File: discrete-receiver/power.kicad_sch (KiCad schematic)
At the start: 67 parts, among them J2 Optional 5V DC Jack, U11 Ag9905LP, U13 LM66100DCK, U14 LM66100DCK, U15 LM66100DCK

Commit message: Add components
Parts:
- removed R3: 49.9kΩ, PCM_JLCPCB:R_0402, symbol PCM_JLCPCB-Resistors:0402,49.9kΩ
- added C105: 100nF, PCM_JLCPCB:C_0402, symbol PCM_JLCPCB-Capacitors:0402,100nF
- added R3: 47kΩ, PCM_JLCPCB:R_0402, symbol PCM_JLCPCB-Resistors:0402,47kΩ
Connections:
- net at R10.1, U20.3 (FB): now also R3.2
- net at JP30.2 (B), R27.1, U20.1 (OUT)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: now also C105.2, R3.1
- net at C95.2, R27.2, R35.1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: now also C105.1

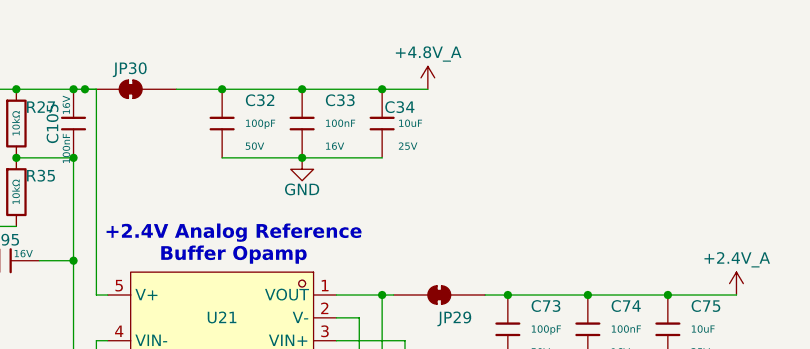
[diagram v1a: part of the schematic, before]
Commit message: shrinked PCB; left digital for peter to finish
The PCB has been shrunk to appropriate size for JLCPCB not adding additional charges. I've left the digital section for Peter to shrink and put in the bound of the board.
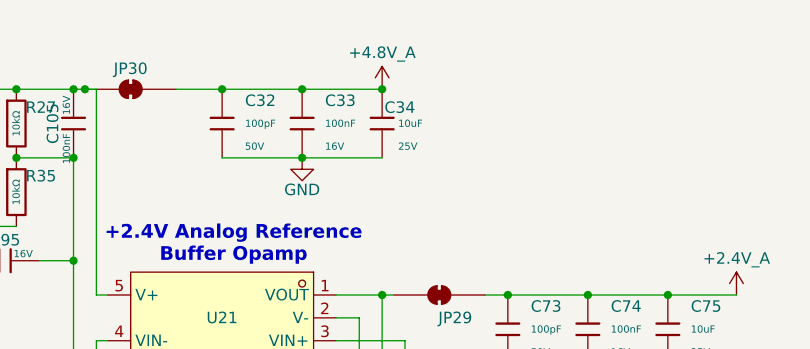
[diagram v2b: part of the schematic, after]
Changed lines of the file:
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@@
 	)
 	(junction
-		(at 181.61 36.83)
-		(diameter 0)
-		(color 0 0 0 0)
-	)
-	(junction
 		(at 115.57 55.88)
 		(diameter 0)
@@
 	)
 	(junction
+		(at 181.61 36.83)
+		(diameter 0)
+		(color 0 0 0 0)
+	)
+	(junction
 		(at 163.83 125.73)
 		(diameter 0)
@@
 	(wire
 		(pts
-			(xy 181.61 36.83) (xy 186.69 36.83)
-		)
-		(stroke
-			(width 0)
-			(type default)
-		)
-	)
-	(wire
-		(pts
 			(xy 147.32 36.83) (xy 148.59 36.83)
 		)
@@
 	(symbol
 		(lib_id "power:+5V")
-		(at 186.69 36.83 0)
+		(at 181.61 36.83 0)
 		(unit 1)
 		(body_style 1)
@@
 		(dnp no)
 		(property "Reference" "#PWR0119"
-			(at 186.69 40.64 0)
+			(at 181.61 40.64 0)
 			(hide yes)
 			(show_name no)
@@
 		)
 		(property "Value" "+4.8V_A"
-			(at 186.69 32.766 0)
+			(at 181.61 32.766 0)
 			(show_name no)
 			(do_not_autoplace no)
@@
 		)
 		(property "Footprint" ""
-			(at 186.69 36.83 0)
+			(at 181.61 36.83 0)
 			(hide yes)
 			(show_name no)
@@
 		)
 		(property "Datasheet" ""
-			(at 186.69 36.83 0)
+			(at 181.61 36.83 0)
 			(hide yes)
 			(show_name no)
@@
 		)
 		(property "Description" "Power symbol creates a global label with name \"+5V\""
-			(at 186.69 36.83 0)
+			(at 181.61 36.83 0)
 			(hide yes)
 			(show_name no)

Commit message: insurance commit
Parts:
- U13, U14, U15: LCSC (none) -> C2832141
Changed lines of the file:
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@@
 			)
 		)
+		(property "LCSC" "C2832141"
+			(at 83.82 110.49 0)
+			(hide yes)
+			(show_name no)
+			(do_not_autoplace no)
+			(effects
+				(font
+					(size 1.27 1.27)
+				)
+			)
+		)
 		(pin "6"
 		)
@@
 		(dnp no)
 		(property "Reference" "R3"
-			(at 136.144 39.37 0)
+			(at 136.652 41.91 90)
 			(show_name no)
 			(do_not_autoplace no)
@@
 			)
 		)
+		(property "LCSC" "C2832141"
+			(at 83.82 133.35 0)
+			(hide yes)
+			(show_name no)
+			(do_not_autoplace no)
+			(effects
+				(font
+					(size 1.27 1.27)
+				)
+			)
+		)
 		(pin "6"
 		)
@@
 		(dnp no)
 		(property "Reference" "R10"
-			(at 135.636 46.482 0)
+			(at 136.906 50.038 90)
 			(show_name no)
 			(do_not_autoplace no)
@@
 			)
 		)
+		(property "LCSC" "C2832141"
+			(at 83.82 87.63 0)
+			(hide yes)
+			(show_name no)
+			(do_not_autoplace no)
+			(effects
+				(font
+					(size 1.27 1.27)
+				)
+			)
+		)
 		(pin "6"
 		)
@@
 		(dnp no)
 		(property "Reference" "R35"
-			(at 141.986 46.482 0)
+			(at 143.002 50.038 90)
 			(show_name no)
 			(do_not_autoplace no)
@@
 		(dnp no)
 		(property "Reference" "R27"
-			(at 141.986 38.862 0)
+			(at 143.002 42.418 90)
 			(show_name no)
 			(do_not_autoplace no)
@@
 		(dnp no)
 		(property "Reference" "C34"
-			(at 181.864 38.862 0)
+			(at 183.134 40.64 0)
 			(show_name no)
 			(do_not_autoplace no)
@@
 		)
 		(property "Value" "10uF"
-			(at 183.388 40.6401 0)
+			(at 181.61 39.37 0)
 			(show_name no)
 			(do_not_autoplace no)
@@
 		)
 		(property "Voltage Rated" "25V"
-			(at 183.388 43.1801 0)
+			(at 182.118 42.164 0)
 			(show_name no)
 			(do_not_autoplace no)
@@
 		(in_pos_files yes)
 		(dnp no)
-		(fields_autoplaced yes)
 		(property "Reference" "C33"
-			(at 175.26 38.0999 0)
+			(at 174.244 40.64 0)
 			(show_name no)
 			(do_not_autoplace no)
@@
 		)
 		(property "Value" "100nF"
-			(at 175.26 40.64 0)
+			(at 172.72 39.116 0)
 			(show_name no)
 			(do_not_autoplace no)
@@
 		)
 		(property "Voltage Rated" "16V"
-			(at 175.26 43.18 0)
+			(at 172.974 42.164 0)
 			(show_name no)
 			(do_not_autoplace no)
@@
 		(dnp no)
 		(property "Reference" "C105"
-			(at 145.034 40.64 90)
+			(at 145.288 40.894 90)
 			(show_name no)
 			(do_not_autoplace no)
@@
 		(in_pos_files yes)
 		(dnp no)
-		(fields_autoplaced yes)
 		(property "Reference" "C32"
-			(at 166.37 38.0999 0)
+			(at 165.354 40.64 0)
 			(show_name no)
 			(do_not_autoplace no)
@@
 		)
 		(property "Value" "100pF"
-			(at 166.37 40.64 0)
+			(at 164.084 39.116 0)
 			(show_name no)
 			(do_not_autoplace no)
@@
 		)
 		(property "Voltage Rated" "50V"
-			(at 166.37 43.18 0)
+			(at 164.084 42.164 0)
 			(show_name no)
 			(do_not_autoplace no)

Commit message: Updated JLC part numbers because some parts were out of stock
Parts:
- U12, U22, U8: LCSC (none) -> C500795; LCSC Part Name 800mA、低噪声、低静态电流、高电源抑制比、低压差线性稳压器 -> (none); Supplier LCSC -> (none); Supplier Part C3294699 -> (none)
- U20: LCSC (none) -> C22392180; LCSC Part Name 800mV~6V 1A 6V -> (none); Supplier LCSC -> (none); Supplier Part C22392180 -> (none)
- U21: LCSC (none) -> C237000; LCSC Part Name 精密运放RS8551XF -> (none); Supplier LCSC -> (none); Supplier Part C237000 -> (none)
- U23: LCSC (none) -> C500795; LCSC Part Name 800mA、低噪声、低静态电流、高电源抑制比、低压差线性稳压器 -> (none); Manufacturer SGMICRO(圣邦微) -> (none); Manufacturer Part SGM2212-3.3XKC3G/TR -> (none); Supplier LCSC -> (none); Supplier Part C3294699 -> (none)
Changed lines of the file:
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@@
 			)
 		)
-		(property "Supplier Part" "C3294699"
-			(at 128.27 118.11 0)
-			(hide yes)
-			(show_name no)
-			(do_not_autoplace no)
-			(effects
-				(font
-					(size 1.27 1.27)
-				)
-			)
-		)
-		(property "Supplier" "LCSC"
-			(at 128.27 118.11 0)
-			(hide yes)
-			(show_name no)
-			(do_not_autoplace no)
-			(effects
-				(font
-					(size 1.27 1.27)
-				)
-			)
-		)
-		(property "LCSC Part Name" "800mA、低噪声、低静态电流、高电源抑制比、低压差线性稳压器"
+		(property "LCSC" "C500795"
 			(at 128.27 118.11 0)
 			(hide yes)
@@
 			)
 		)
-		(property "Manufacturer Part" "SGM2212-3.3XKC3G/TR"
-			(at 128.27 137.16 0)
-			(hide yes)
-			(show_name no)
-			(do_not_autoplace no)
-			(effects
-				(font
-					(size 1.27 1.27)
-				)
-			)
-		)
-		(property "Manufacturer" "SGMICRO(圣邦微)"
-			(at 128.27 137.16 0)
-			(hide yes)
-			(show_name no)
-			(do_not_autoplace no)
-			(effects
-				(font
-					(size 1.27 1.27)
-				)
-			)
-		)
-		(property "Supplier Part" "C3294699"
-			(at 128.27 137.16 0)
-			(hide yes)
-			(show_name no)
-			(do_not_autoplace no)
-			(effects
-				(font
-					(size 1.27 1.27)
-				)
-			)
-		)
-		(property "Supplier" "LCSC"
-			(at 128.27 137.16 0)
-			(hide yes)
-			(show_name no)
-			(do_not_autoplace no)
-			(effects
-				(font
-					(size 1.27 1.27)
-				)
-			)
-		)
-		(property "LCSC Part Name" "800mA、低噪声、低静态电流、高电源抑制比、低压差线性稳压器"
+		(property "LCSC" "C500795"
 			(at 128.27 137.16 0)
 			(hide yes)
@@
 			)
 		)
-		(property "Supplier Part" "C3294699"
-			(at 128.27 81.28 0)
-			(hide yes)
-			(show_name no)
-			(do_not_autoplace no)
-			(effects
-				(font
-					(size 1.27 1.27)
-				)
-			)
-		)
-		(property "Supplier" "LCSC"
-			(at 128.27 81.28 0)
-			(hide yes)
-			(show_name no)
-			(do_not_autoplace no)
-			(effects
-				(font
-					(size 1.27 1.27)
-				)
-			)
-		)
-		(property "LCSC Part Name" "800mA、低噪声、低静态电流、高电源抑制比、低压差线性稳压器"
+		(property "LCSC" "C500795"
 			(at 128.27 81.28 0)
 			(hide yes)
@@
 			)
 		)
-		(property "Supplier Part" "C237000"
-			(at 163.83 62.23 0)
-			(hide yes)
-			(show_name no)
-			(do_not_autoplace no)
-			(effects
-				(font
-					(size 1.27 1.27)
-				)
-			)
-		)
-		(property "Supplier" "LCSC"
-			(at 163.83 62.23 0)
-			(hide yes)
-			(show_name no)
-			(do_not_autoplace no)
-			(effects
-				(font
-					(size 1.27 1.27)
-				)
-			)
-		)
-		(property "LCSC Part Name" "精密运放RS8551XF"
+		(property "LCSC" "C237000"
 			(at 163.83 62.23 0)
 			(hide yes)
@@
 			)
 		)
-		(property "Supplier Part" "C3294699"
-			(at 128.27 100.33 0)
-			(hide yes)
-			(show_name no)
-			(do_not_autoplace no)
-			(effects
-				(font
-					(size 1.27 1.27)
-				)
-			)
-		)
-		(property "Supplier" "LCSC"
-			(at 128.27 100.33 0)
-			(hide yes)
-			(show_name no)
-			(do_not_autoplace no)
-			(effects
-				(font
-					(size 1.27 1.27)
-				)
-			)
-		)
-		(property "LCSC Part Name" "800mA、低噪声、低静态电流、高电源抑制比、低压差线性稳压器"
+		(property "LCSC" "C500795"
 			(at 128.27 100.33 0)
 			(hide yes)
@@
 			)
 		)
-		(property "Supplier Part" "C22392180"
-			(at 116.84 45.72 0)
-			(hide yes)
-			(show_name no)
-			(do_not_autoplace no)
-			(effects
-				(font
-					(size 1.27 1.27)
-				)
-			)
-		)
-		(property "Supplier" "LCSC"
-			(at 116.84 45.72 0)
-			(hide yes)
-			(show_name no)
-			(do_not_autoplace no)
-			(effects
-				(font
-					(size 1.27 1.27)
-				)
-			)
-		)
-		(property "LCSC Part Name" "800mV~6V 1A 6V"
+		(property "LCSC" "C22392180"
 			(at 116.84 45.72 0)
 			(hide yes)

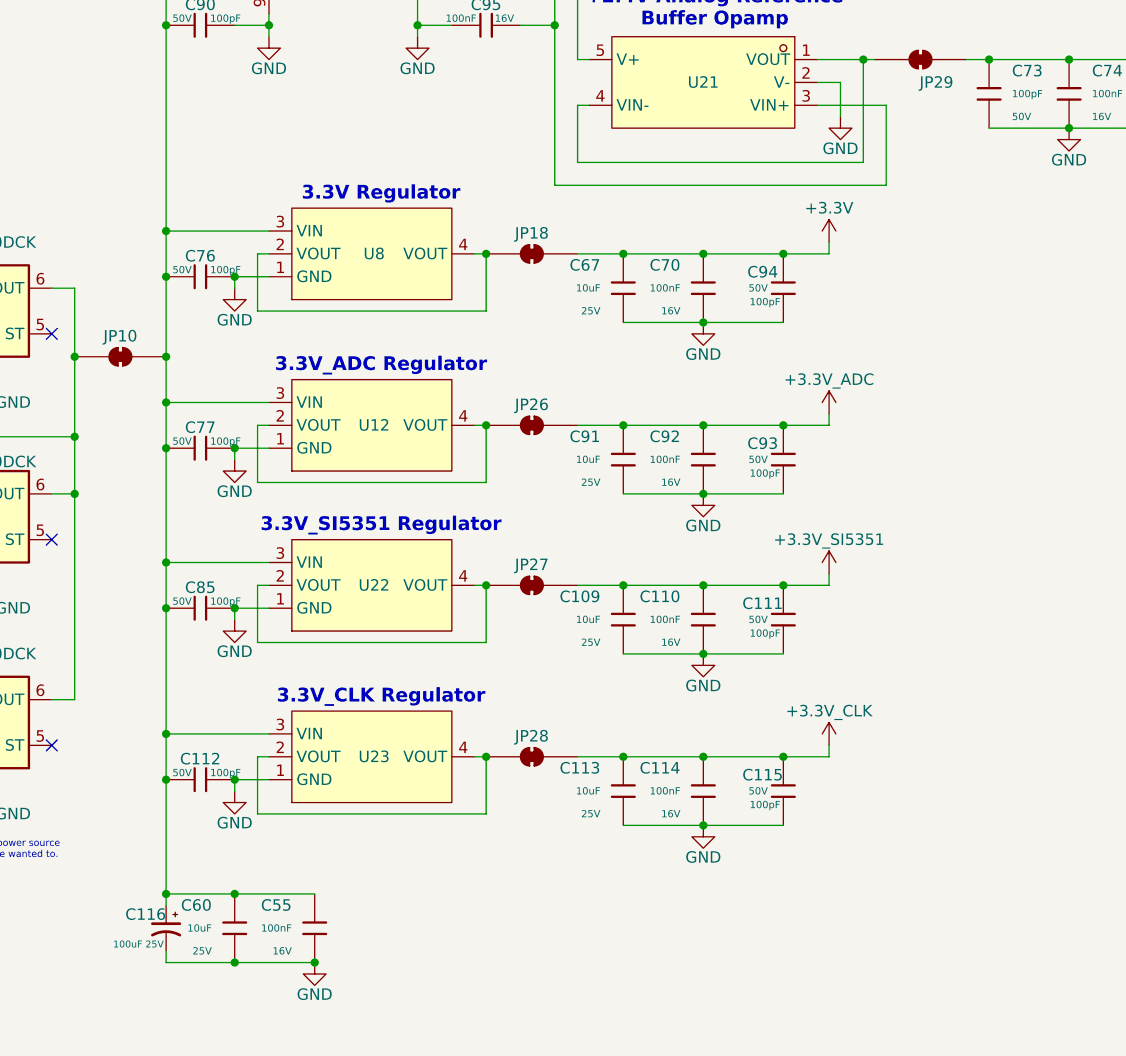
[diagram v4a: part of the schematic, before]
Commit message: Replaced 3.3V regulators 😠
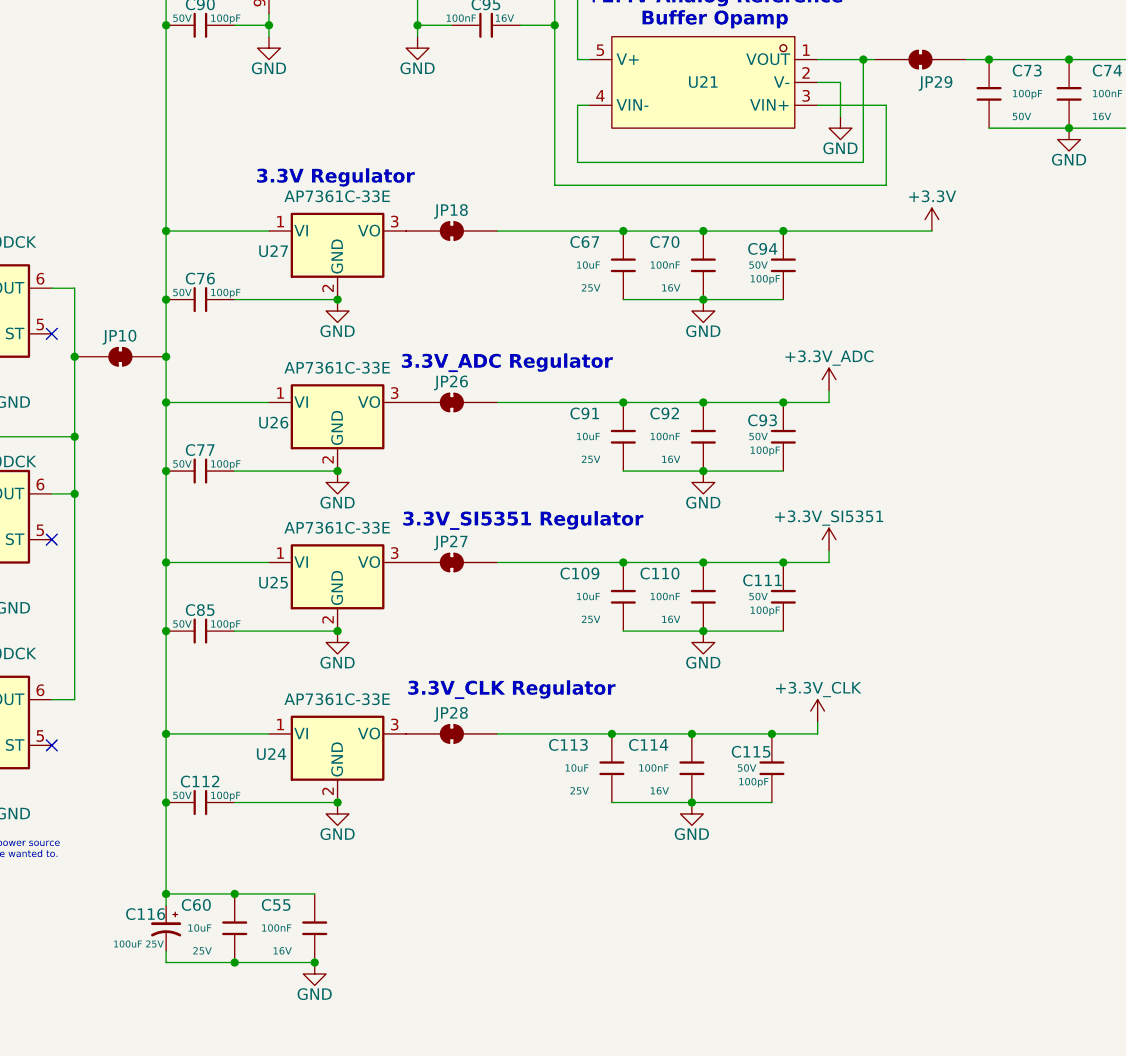
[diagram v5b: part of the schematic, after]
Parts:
- removed U12, U22, U23, U8: (no value), EasyEDA_Lib:SOT-223-3_L6.5-W3.4-P2.30-LS7.0-BR, symbol EasyEDA_Lib:SGM2212-3.3XKC3G/TR_C3294699
- added U24, U25, U26, U27: AP7361C-33E, Package_TO_SOT_SMD:SOT-223-3_TabPin2, symbol Regulator_Linear:AP7361C-33E
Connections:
- net +5V: now also U24.1 (VI), U25.1 (VI), U26.1 (VI), U27.1 (VI)
- net GND: now also U24.2 (GND), U25.2 (GND), U26.2 (GND), U27.2 (GND)
- net at JP27.2 (B): now also U25.3 (VO)
- net at JP28.2 (B): now also U24.3 (VO)
- net at JP18.2 (B): now also U27.3 (VO)
- net at JP26.2 (B): now also U26.3 (VO)
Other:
- moved on the sheet: C109, C110, C111, C112, C113, C114, C115, C67, C70, C76, C77, C85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

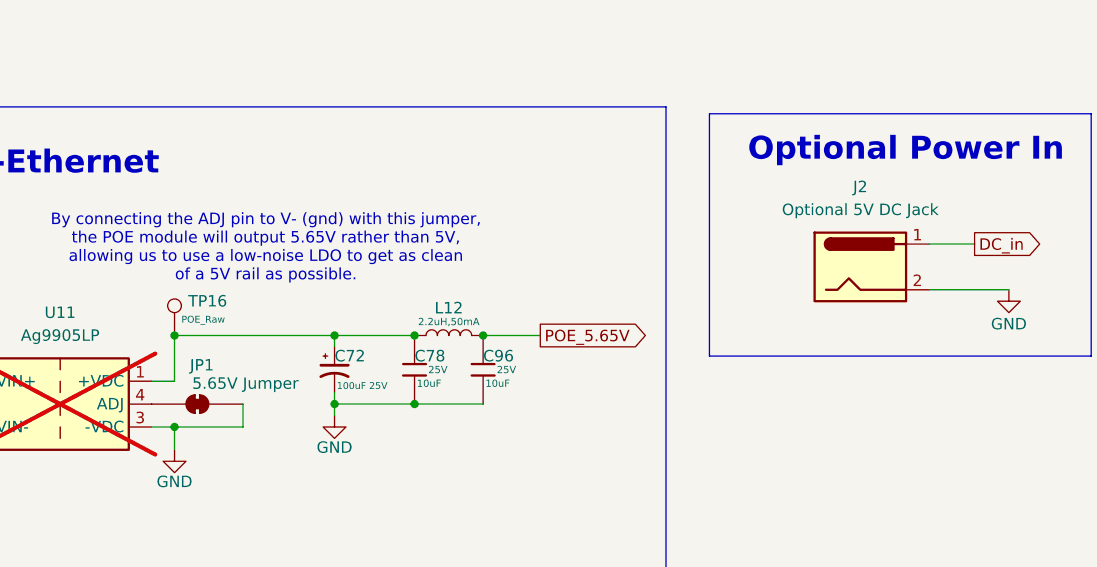
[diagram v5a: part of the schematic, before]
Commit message: Updated PCB DNP field for some parts
made pin headers and a few of the connectors DNP
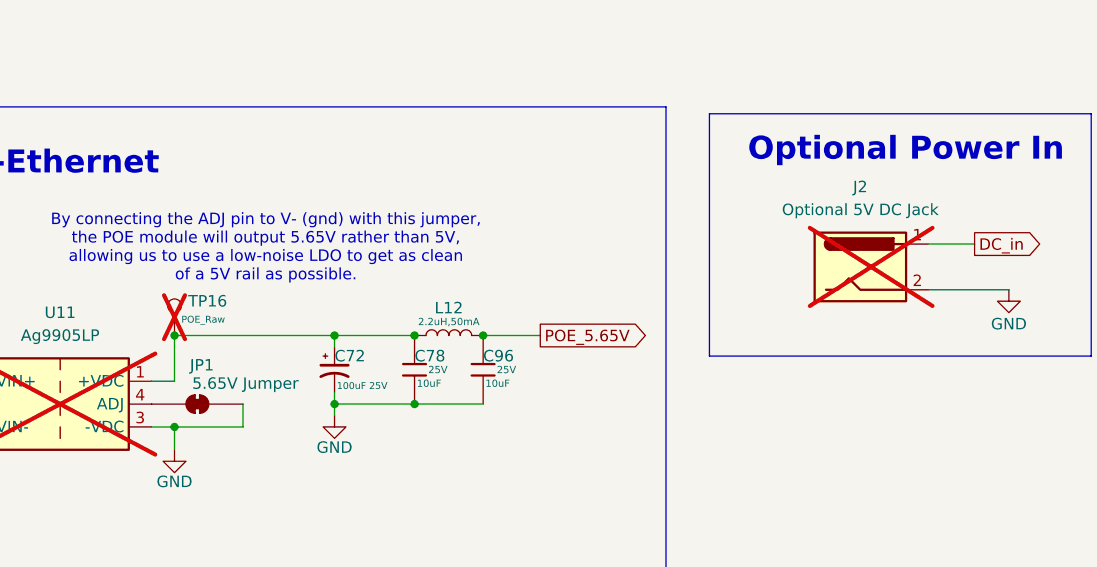
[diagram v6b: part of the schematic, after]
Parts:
- J2, TP16: now not fitted; now left out of the parts list
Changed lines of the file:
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@@
 		(body_style 1)
 		(exclude_from_sim no)
-		(in_bom yes)
+		(in_bom no)
 		(on_board yes)
-		(in_pos_files yes)
-		(dnp no)
+		(in_pos_files no)
+		(dnp yes)
 		(fields_autoplaced yes)
 		(property "Reference" "J2"
@@
 		(body_style 1)
 		(exclude_from_sim no)
-		(in_bom yes)
+		(in_bom no)
 		(on_board yes)
-		(in_pos_files yes)
-		(dnp no)
+		(in_pos_files no)
+		(dnp yes)
 		(property "Reference" "TP16"
 			(at 150.114 243.84 0)

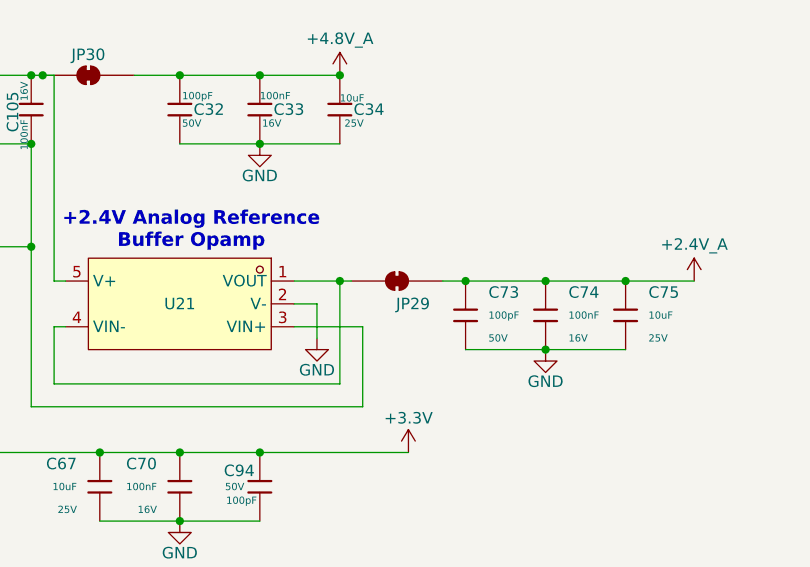
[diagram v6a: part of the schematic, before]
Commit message: replaced RJ45 connector 😡🙄🥀
The original was too expensive from JLCPCB and Digikey.
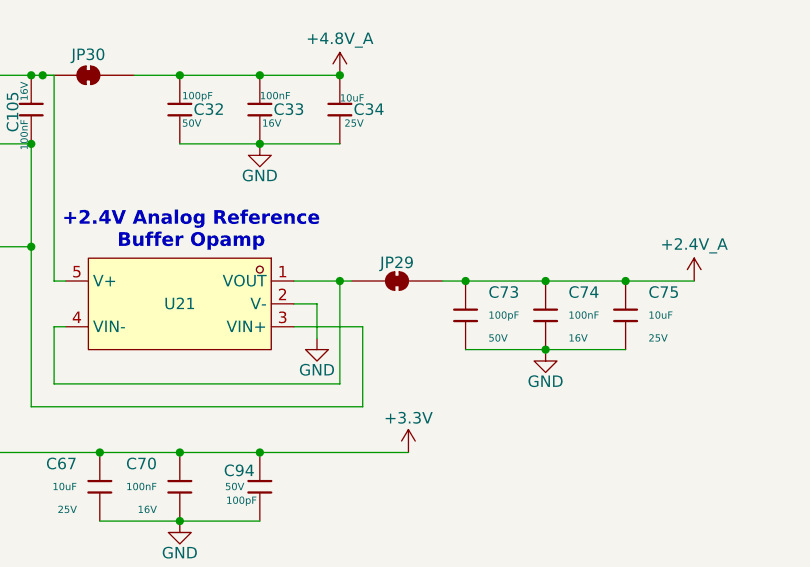
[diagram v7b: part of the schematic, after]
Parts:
- D3, D4: AVAILABILITY Unavailable -> (none); LCSC (none) -> C361576
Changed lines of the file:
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@@
 			)
 		)
-		(property "AVAILABILITY" "Unavailable"
+		(property "LCSC" "C361576"
 			(at 88.9 245.11 0)
 			(hide yes)
@@
 		(in_bom no)
 		(on_board yes)
-		(in_pos_files yes)
+		(in_pos_files no)
 		(dnp no)
 		(property "Reference" "JP29"
-			(at 189.738 62.23 0)
+			(at 187.96 57.658 0)
 			(show_name no)
 			(do_not_autoplace no)
@@
 		(in_bom no)
 		(on_board yes)
-		(in_pos_files yes)
+		(in_pos_files no)
 		(dnp no)
 		(property "Reference" "JP18"
@@
 		(in_bom no)
 		(on_board yes)
-		(in_pos_files yes)
+		(in_pos_files no)
 		(dnp no)
 		(property "Reference" "JP7"
@@
 			)
 		)
-		(property "AVAILABILITY" "Unavailable"
+		(property "LCSC" " C361576"
 			(at 88.9 266.7 0)
 			(hide yes)
@@
 		(in_bom no)
 		(on_board yes)
-		(in_pos_files yes)
+		(in_pos_files no)
 		(dnp no)
 		(property "Reference" "JP28"
@@
 		(in_bom no)
 		(on_board yes)
-		(in_pos_files yes)
+		(in_pos_files no)
 		(dnp no)
 		(property "Reference" "JP30"
@@
 		(in_bom no)
 		(on_board yes)
-		(in_pos_files yes)
+		(in_pos_files no)
 		(dnp no)
 		(property "Reference" "JP8"
@@
 		(in_bom no)
 		(on_board yes)
-		(in_pos_files yes)
+		(in_pos_files no)
 		(dnp no)
 		(property "Reference" "JP10"
@@
 		(in_bom no)
 		(on_board yes)
-		(in_pos_files yes)
+		(in_pos_files no)
 		(dnp no)
 		(property "Reference" "JP27"
@@
 		(in_bom no)
 		(on_board yes)
-		(in_pos_files yes)
+		(in_pos_files no)
 		(dnp no)
 		(property "Reference" "JP1"
@@
 		(in_bom no)
 		(on_board yes)
-		(in_pos_files yes)
+		(in_pos_files no)
 		(dnp no)
 		(property "Reference" "JP26"
@@
 		(in_bom no)
 		(on_board yes)
-		(in_pos_files yes)
+		(in_pos_files no)
 		(dnp no)
 		(property "Reference" "JP9"
